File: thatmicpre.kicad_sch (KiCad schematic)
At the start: 12 parts, among them J1 Conn_01x07_Female, U1 THAT1512P08-U

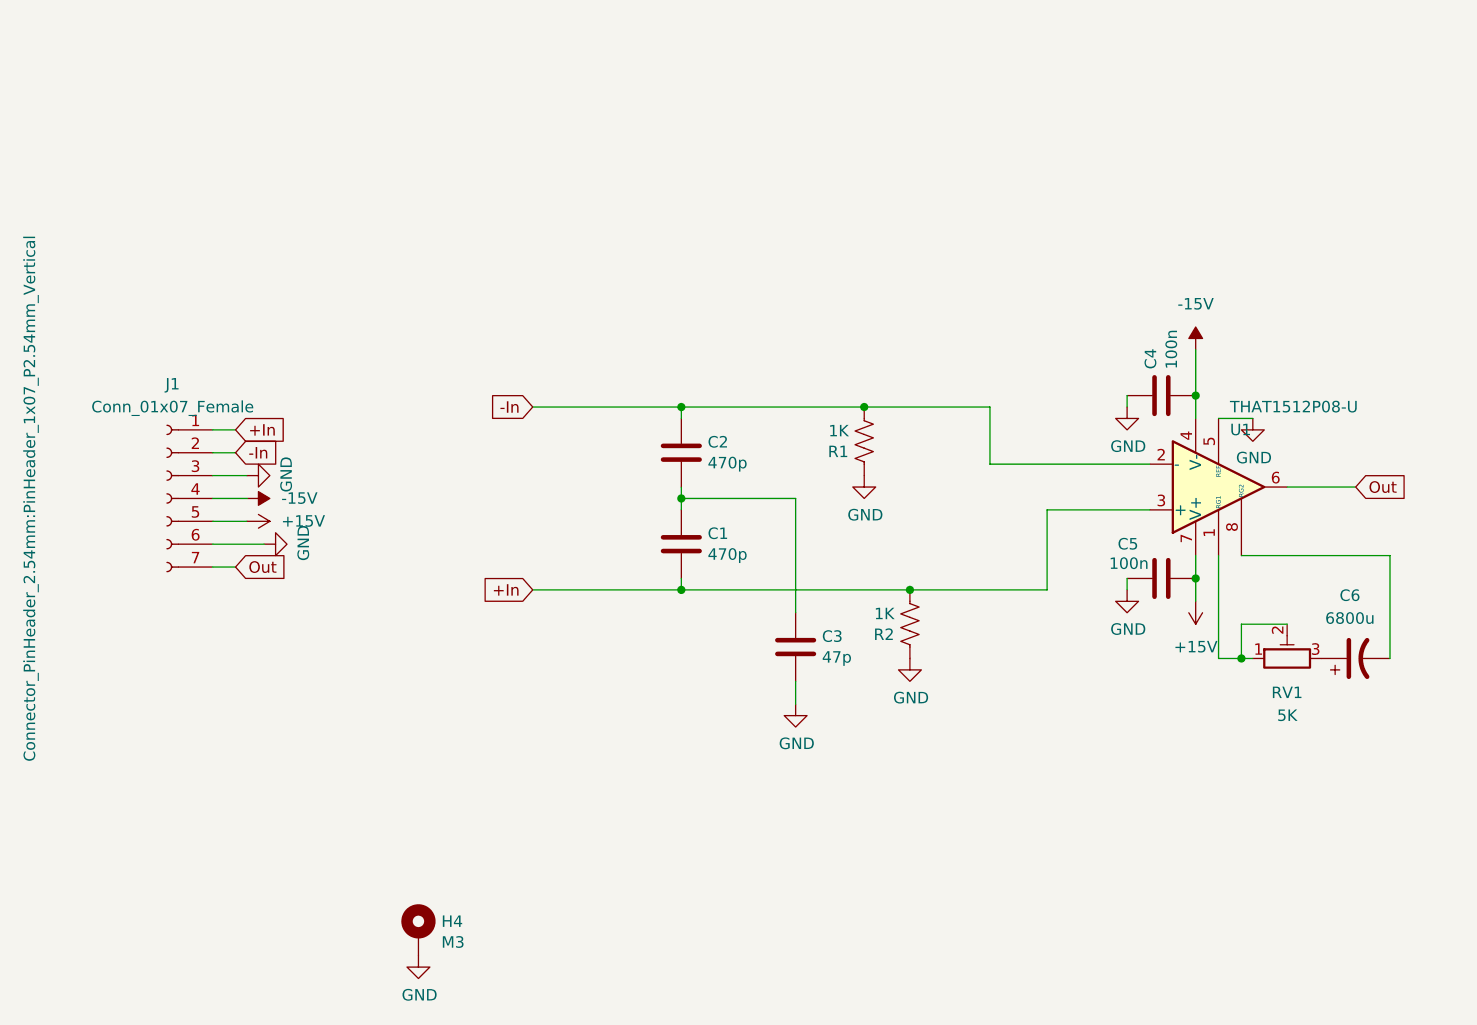
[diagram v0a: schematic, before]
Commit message: Migrate schematic and board to KiCad 10 format; drop the KiCad 5 .pro
kicad-cli sch/pcb upgrade only. Exported netlist identical before and
after; DRC violations identical. thatmicpre-rounded.kicad_pcb is left as
rev2's derived fab file and is regenerated once rev3 is laid out.

Co-Authored-By: Claude Opus 5.5 <noreply@anthropic.com>
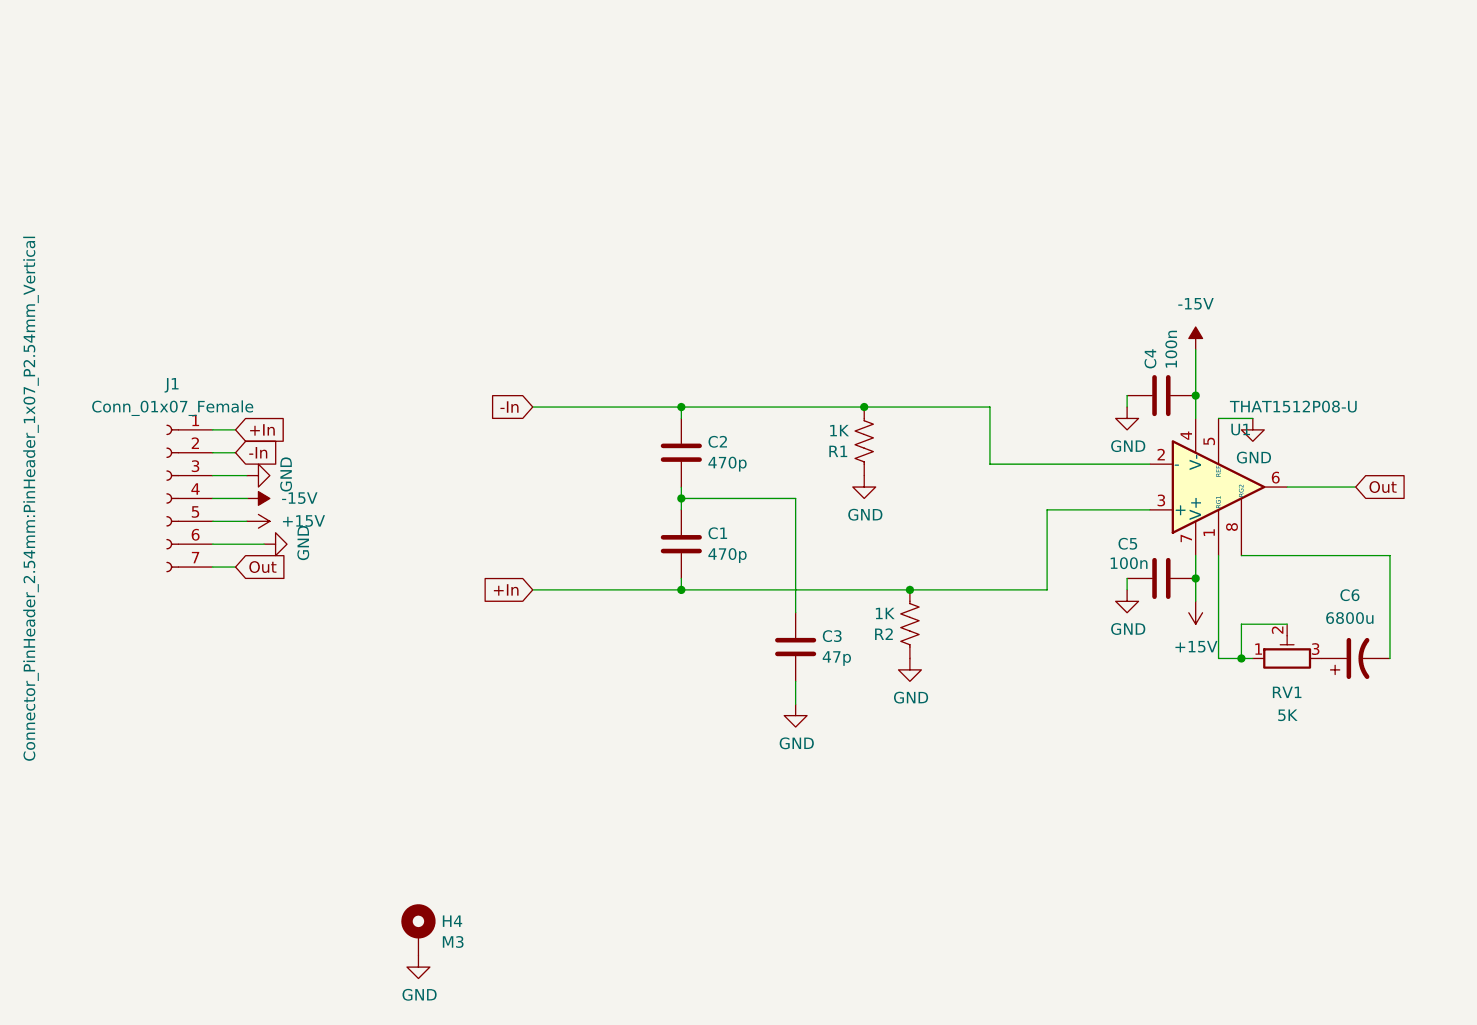
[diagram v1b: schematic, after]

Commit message: rev3 schematic: correct part numbers, output and rail resistors, gain stop
Part-number (Vendor) fields that named the wrong part:
- U1 THAT1510P08-U -> THAT1512P08-U (the 1510 has a different gain law)
- C4, C5 (100n) carried the 470 pF RDE5C2A471...; now RDER71H104K0M1H03A
- R1, R2 (1k) carried a 6.81 k CMF556K8100BEEK; now CMF551K0000BEEK
- RV1 value 5K -> 1K, matching the board and README; 3362P-1-102LF
- C6 had no footprint in the schematic; now CP_Radial_D12.5mm_P5.00mm

Added:
- R3 100R build-out between U1 pin 6 and Out (cable capacitance;
  THAT1512 is specified to 300 pF)
- R6 5R6 in series with RV1 and C6: defines the top of the gain range
  (~59 dB with RV1 at zero) instead of leaving it to trimmer end resistance
- R4/C7, R5/C8: 10R + 10u per rail at the connector; U1 and its 100n now
  sit on +15V_F / -15V_F
- PWR_FLAGs on GND, +-15V and +-15V_F: ERC errors 3 -> 0

Title block rev 3, 2026-10-03, set through eeschema's Page Settings. That
save also replaced the KiCad 6 symbol_instances table, which kicad-cli's
upgrade had left in place and which Konnect refuses to edit, with
per-symbol instances; netlist unchanged across it. The stale rev2 rounded
board and its project are dropped (kept in tag rev2): their second
.kicad_pro made Konnect refuse the directory as ambiguous.

No output coupling cap: card 10 already AC-couples after T.P.1 (C1
0.05u), and C6 holds the THAT1512 at DC gain 1/2, so offset stays ~5 mV.

Co-Authored-By: Claude Opus 5.5 <noreply@anthropic.com>
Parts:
- added C7, C8: 10u, Capacitor_THT:CP_Radial_D5.0mm_P2.00mm, symbol Device:C_Polarized_US
- added R3: 100R, Resistor_THT:R_Axial_DIN0204_L3.6mm_D1.6mm_P2.54mm_Vertical, symbol Device:R_US
- added R4, R5: 10R, Resistor_THT:R_Axial_DIN0204_L3.6mm_D1.6mm_P2.54mm_Vertical, symbol Device:R_US
- added R6: 5R6, Resistor_THT:R_Axial_DIN0207_L6.3mm_D2.5mm_P2.54mm_Vertical, symbol Device:R_US
- C4, C5: Vendor RDE5C2A471J0M1H03A -> RDER71H104K0M1H03A
- C6: footprint (none) -> Capacitor_THT:CP_Radial_D12.5mm_P5.00mm
- J1: value Conn_01x07_Female -> PinHeader_1x07
- R1, R2: Vendor CMF556K8100BEEK -> CMF551K0000BEEK
- RV1: value 5K -> 1K; Vendor (none) -> 3362P-1-102LF
- U1: Vendor THAT1510P08-U -> THAT1512P08-U
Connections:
- net +15V: now also R4.1; no longer C5.2, U1.7 (V+)
- net -15V: now also R5.1; no longer C4.2, U1.4 (V-)
- net GND: now also C7.2, C8.1
- net Out: now also R3.2; no longer U1.6
- net at C6.1: now also R6.2; no longer RV1.3
- new net: R3.1, U1.6
- new net: R6.1, RV1.3
- new net +15V_F: C5.2, C7.1, R4.2, U1.7 (V+)
- new net -15V_F: C4.2, C8.2, R5.2, U1.4 (V-)
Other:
- moved on the sheet: C6
